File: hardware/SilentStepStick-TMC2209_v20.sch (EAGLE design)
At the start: 25 parts, among them IC2 TMC2209-LA, J1 MA08-1, J2 MA08-1, J3 MA02-1, X1 PASSER-04, X2 PASSER-04

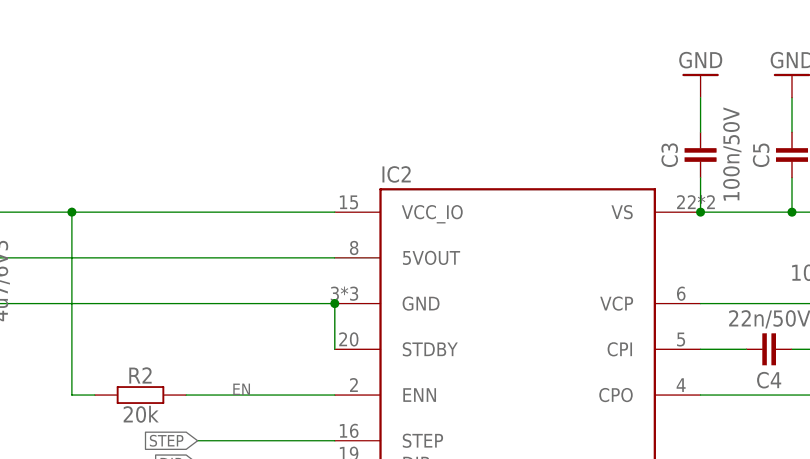
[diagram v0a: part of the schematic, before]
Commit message: updated schematics
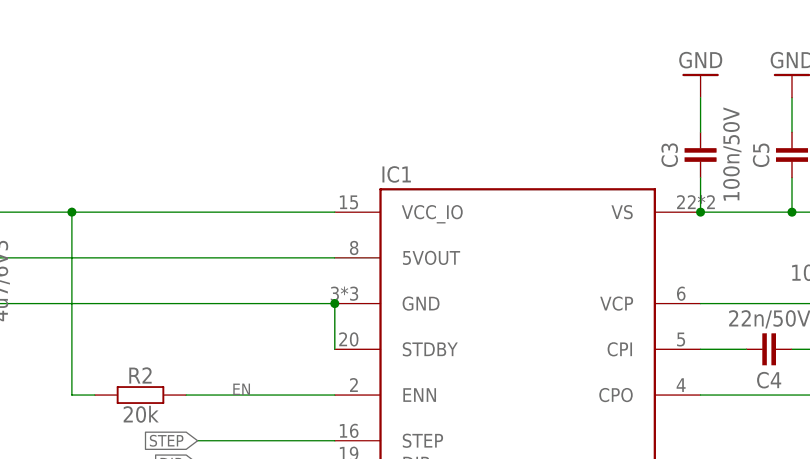
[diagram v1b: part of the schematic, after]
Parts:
- renumbered IC2 to IC1
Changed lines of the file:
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@@
 <part name="REF" library="we-rcl" deviceset="PAD" device="-0.6-1.1" value="PAD-0.6-1.1"/>
 <part name="C7B" library="rcl" deviceset="C-EU" device="C1206" value="10u/35V"/>
-<part name="IC2" library="we-chip" deviceset="TMC2209" device="-LA"/>
+<part name="IC1" library="we-chip" deviceset="TMC2209" device="-LA"/>
 <part name="J1" library="we-con" deviceset="MA08-1" device=""/>
 <part name="C8" library="rcl" deviceset="C-EU" device="C1206" value="10u/35V"/>
@@
 <attribute name="VALUE" x="152.4" y="156.21" size="1.778" layer="96" rot="R90"/>
 </instance>
-<instance part="IC2" gate="IC" x="105.41" y="118.11"/>
+<instance part="IC1" gate="IC" x="105.41" y="118.11"/>
 <instance part="J1" gate="J" x="189.23" y="142.24"/>
 <instance part="C8" gate="G$1" x="162.56" y="153.67" smashed="yes" rot="R180">
@@
 <segment>
 <label x="69.85" y="115.57" size="1.27" layer="95" rot="R180" xref="yes"/>
-<pinref part="IC2" gate="IC" pin="DIAG"/>
+<pinref part="IC1" gate="IC" pin="DIAG"/>
 <wire x1="85.09" y1="115.57" x2="69.85" y2="115.57" width="0.1524" layer="91"/>
 </segment>
@@
 <segment>
 <label x="69.85" y="113.03" size="1.27" layer="95" rot="R180" xref="yes"/>
-<pinref part="IC2" gate="IC" pin="INDEX"/>
+<pinref part="IC1" gate="IC" pin="INDEX"/>
 <wire x1="85.09" y1="113.03" x2="69.85" y2="113.03" width="0.1524" layer="91"/>
 </segment>
@@
 <segment>
 <label x="69.85" y="123.19" size="1.27" layer="95" rot="R180" xref="yes"/>
-<pinref part="IC2" gate="IC" pin="STEP"/>
+<pinref part="IC1" gate="IC" pin="STEP"/>
 <wire x1="85.09" y1="123.19" x2="69.85" y2="123.19" width="0.1524" layer="91"/>
 </segment>
@@
 <segment>
 <label x="69.85" y="120.65" size="1.27" layer="95" rot="R180" xref="yes"/>
-<pinref part="IC2" gate="IC" pin="DIR"/>
+<pinref part="IC1" gate="IC" pin="DIR"/>
 <wire x1="85.09" y1="120.65" x2="69.85" y2="120.65" width="0.1524" layer="91"/>
 </segment>
@@
 <junction x="154.94" y="151.13"/>
 <wire x1="154.94" y1="151.13" x2="147.32" y2="151.13" width="0.1524" layer="91"/>
-<pinref part="IC2" gate="IC" pin="VS"/>
+<pinref part="IC1" gate="IC" pin="VS"/>
 <pinref part="C8" gate="G$1" pin="1"/>
 <wire x1="162.56" y1="151.13" x2="154.94" y2="151.13" width="0.1524" layer="91"/>
@@
 <wire x1="44.45" y1="135.89" x2="44.45" y2="138.43" width="0.1524" layer="91"/>
 <junction x="44.45" y="138.43"/>
-<pinref part="IC2" gate="IC" pin="GND"/>
+<pinref part="IC1" gate="IC" pin="GND"/>
 <junction x="85.09" y="138.43"/>
-<pinref part="IC2" gate="IC" pin="STDBY"/>
+<pinref part="IC1" gate="IC" pin="STDBY"/>
 <wire x1="85.09" y1="133.35" x2="85.09" y2="138.43" width="0.1524" layer="91"/>
 </segment>
@@
 <junction x="50.8" y="95.25"/>
 <wire x1="50.8" y1="97.79" x2="85.09" y2="97.79" width="0.1524" layer="91"/>
-<pinref part="IC2" gate="IC" pin="CLK"/>
+<pinref part="IC1" gate="IC" pin="CLK"/>
 </segment>
 <segment>
@@
 <segment>
 <label x="133.35" y="118.11" size="1.27" layer="95" xref="yes"/>
-<pinref part="IC2" gate="IC" pin="OA1"/>
+<pinref part="IC1" gate="IC" pin="OA1"/>
 <wire x1="125.73" y1="118.11" x2="133.35" y2="118.11" width="0.1524" layer="91"/>
 </segment>
@@
 <segment>
 <label x="133.35" y="113.03" size="1.27" layer="95" xref="yes"/>
-<pinref part="IC2" gate="IC" pin="OA2"/>
+<pinref part="IC1" gate="IC" pin="OA2"/>
 <wire x1="125.73" y1="113.03" x2="133.35" y2="113.03" width="0.1524" layer="91"/>
 </segment>
@@
 <segment>
 <label x="133.35" y="102.87" size="1.27" layer="95" xref="yes"/>
-<pinref part="IC2" gate="IC" pin="OB2"/>
+<pinref part="IC1" gate="IC" pin="OB2"/>
 <wire x1="125.73" y1="102.87" x2="133.35" y2="102.87" width="0.1524" layer="91"/>
 </segment>
@@
 <segment>
 <label x="133.35" y="107.95" size="1.27" layer="95" xref="yes"/>
-<pinref part="IC2" gate="IC" pin="OB1"/>
+<pinref part="IC1" gate="IC" pin="OB1"/>
 <wire x1="125.73" y1="107.95" x2="133.35" y2="107.95" width="0.1524" layer="91"/>
 </segment>
@@
 <junction x="55.88" y="148.59"/>
 <junction x="31.75" y="148.59"/>
-<pinref part="IC2" gate="IC" pin="VCC_IO"/>
+<pinref part="IC1" gate="IC" pin="VCC_IO"/>
 </segment>
 </net>
@@
 <segment>
 <pinref part="C6" gate="C" pin="2"/>
-<pinref part="IC2" gate="IC" pin="VCP"/>
+<pinref part="IC1" gate="IC" pin="VCP"/>
 <wire x1="125.73" y1="138.43" x2="138.43" y2="138.43" width="0.1524" layer="91"/>
 </segment>
@@
 <segment>
 <pinref part="C4" gate="C" pin="2"/>
-<pinref part="IC2" gate="IC" pin="CPI"/>
+<pinref part="IC1" gate="IC" pin="CPI"/>
 <wire x1="125.73" y1="133.35" x2="130.81" y2="133.35" width="0.1524" layer="91"/>
 </segment>
@@
 <wire x1="140.97" y1="133.35" x2="135.89" y2="133.35" width="0.1524" layer="91"/>
 <pinref part="C4" gate="C" pin="1"/>
-<pinref part="IC2" gate="IC" pin="CPO"/>
+<pinref part="IC1" gate="IC" pin="CPO"/>
 </segment>
 </net>
@@
 <wire x1="125.73" y1="92.71" x2="140.97" y2="92.71" width="0.1524" layer="91"/>
 <wire x1="140.97" y1="92.71" x2="140.97" y2="86.36" width="0.1524" layer="91"/>
-<pinref part="IC2" gate="IC" pin="BRA"/>
+<pinref part="IC1" gate="IC" pin="BRA"/>
 </segment>
 </net>
@@
 <wire x1="132.08" y1="87.63" x2="132.08" y2="86.36" width="0.1524" layer="91"/>
 <pinref part="R6" gate="G$1" pin="2"/>
-<pinref part="IC2" gate="IC" pin="BRB"/>
+<pinref part="IC1" gate="IC" pin="BRB"/>
 </segment>
 </net>
@@
 <wire x1="44.45" y1="143.51" x2="44.45" y2="161.29" width="0.1524" layer="91"/>
 <pinref part="C2" gate="C" pin="2"/>
-<pinref part="IC2" gate="IC" pin="5VOUT"/>
+<pinref part="IC1" gate="IC" pin="5VOUT"/>
 </segment>
 <segment>
@@
 <label x="64.77" y="87.63" size="1.27" layer="95" rot="R180" xref="yes"/>
 <junction x="73.66" y="87.63"/>
-<pinref part="IC2" gate="IC" pin="VREF"/>
+<pinref part="IC1" gate="IC" pin="VREF"/>
 <wire x1="85.09" y1="87.63" x2="73.66" y2="87.63" width="0.1524" layer="91"/>
 </segment>
@@
 <segment>
 <label x="69.85" y="105.41" size="1.27" layer="95" rot="R180" xref="yes"/>
-<pinref part="IC2" gate="IC" pin="MS1"/>
+<pinref part="IC1" gate="IC" pin="MS1"/>
 <wire x1="85.09" y1="105.41" x2="69.85" y2="105.41" width="0.1524" layer="91"/>
 </segment>
@@
 <segment>
 <label x="69.85" y="102.87" size="1.27" layer="95" rot="R180" xref="yes"/>
-<pinref part="IC2" gate="IC" pin="MS2"/>
+<pinref part="IC1" gate="IC" pin="MS2"/>
 <wire x1="85.09" y1="102.87" x2="69.85" y2="102.87" width="0.1524" layer="91"/>
 </segment>
@@
 <wire x1="68.58" y1="92.71" x2="85.09" y2="92.71" width="0.1524" layer="91"/>
 <label x="73.66" y="92.71" size="1.27" layer="95"/>
-<pinref part="IC2" gate="IC" pin="PDN_UART"/>
+<pinref part="IC1" gate="IC" pin="PDN_UART"/>
 </segment>
 <segment>
@@
 <pinref part="R2" gate="R" pin="2"/>
 <label x="73.66" y="128.27" size="1.27" layer="95"/>
-<pinref part="IC2" gate="IC" pin="ENN"/>
+<pinref part="IC1" gate="IC" pin="ENN"/>
 <wire x1="68.58" y1="128.27" x2="85.09" y2="128.27" width="0.1524" layer="91"/>
 </segment>
@@
 <net name="SPREAD" class="0">
 <segment>
-<pinref part="IC2" gate="IC" pin="SPREAD"/>
+<pinref part="IC1" gate="IC" pin="SPREAD"/>
 <wire x1="85.09" y1="107.95" x2="69.85" y2="107.95" width="0.1524" layer="91"/>
 <label x="69.85" y="107.95" size="1.27" layer="95" rot="R180" xref="yes"/>

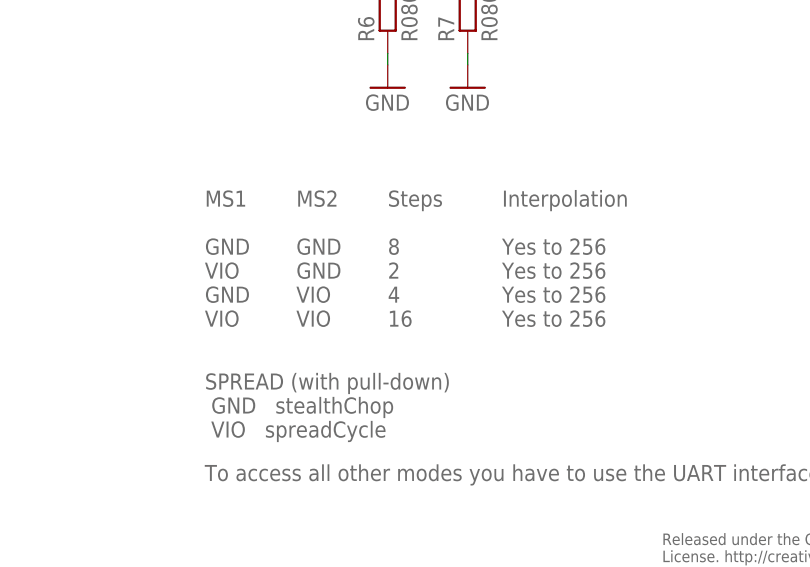
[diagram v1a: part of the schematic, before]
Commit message: updated schematics
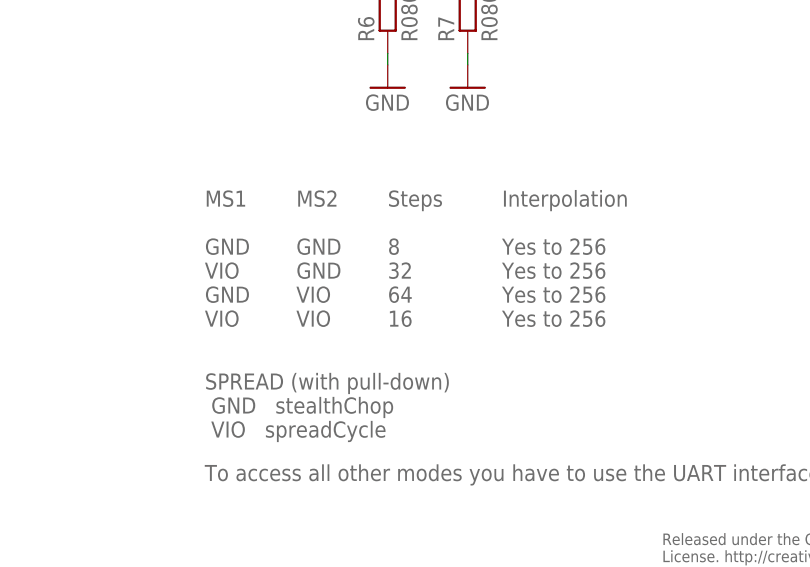
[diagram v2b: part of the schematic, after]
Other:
- note added: "Steps 8 32 64 16"
- note removed: "Steps 8 2 4 16"
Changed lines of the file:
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@@
 <text x="132.08" y="60.96" size="1.778" layer="95" font="vector" ratio="10" align="top-left">Steps
 8
-2
-4
+32
+64
 16
 </text>
